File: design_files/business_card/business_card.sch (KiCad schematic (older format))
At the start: 32 parts, among them J1 Conn_01x06, J2 Conn_01x04_Male, SW3 SW_Push, SW4 SW_Push, U1 ATTINY85-20SU, U2 TLC5940PWP

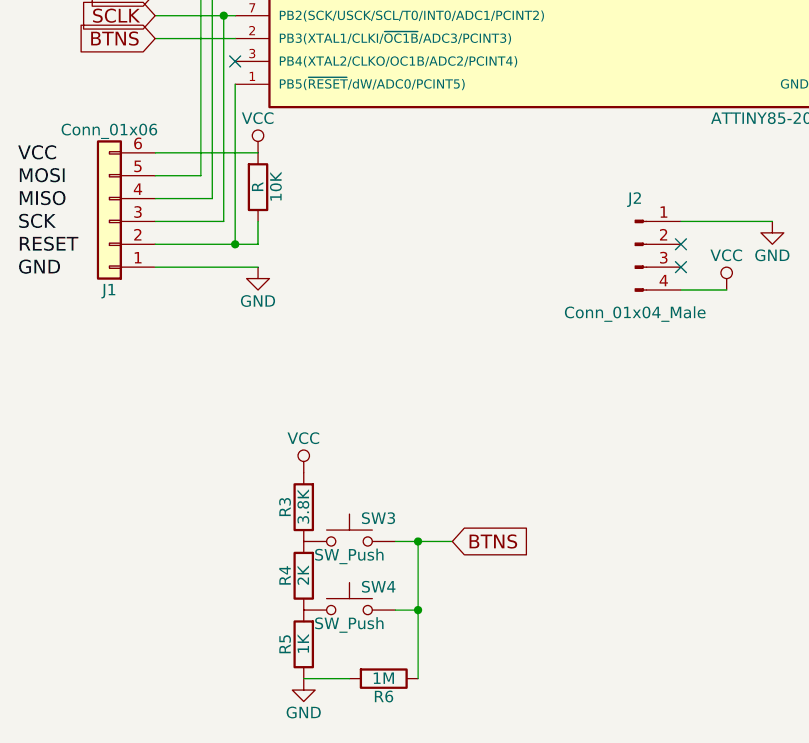
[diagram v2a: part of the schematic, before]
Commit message: progress on configuring 15 leds
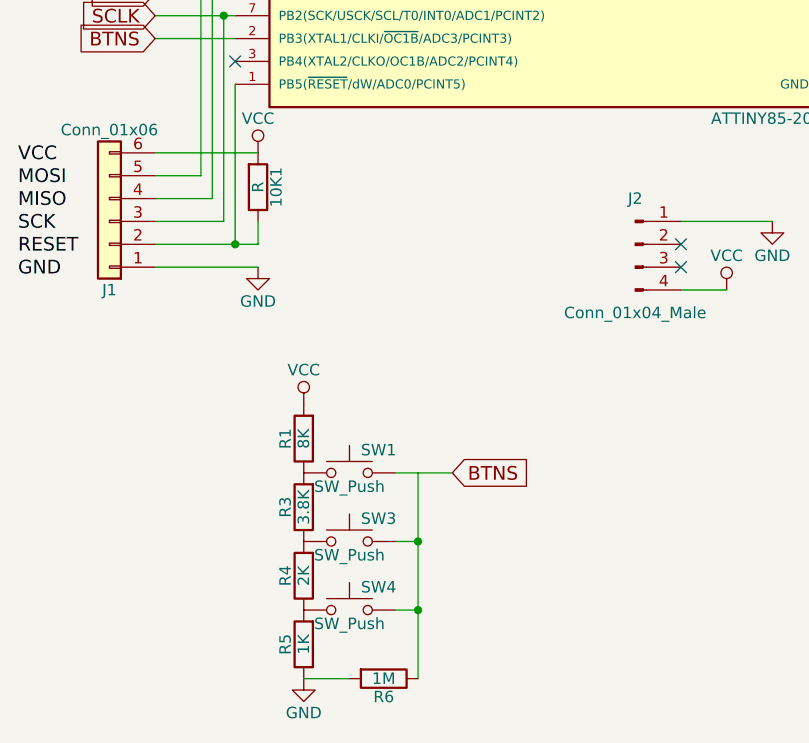
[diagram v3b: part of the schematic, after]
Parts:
- added R1: 8K, Resistors_SMD:R_0805, symbol R
- added SW1: SW_Push, Buttons_Switches_SMD:SW_SPST_SKQG, symbol SW_Push
- renumbered 10K to 10K1
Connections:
- net BTNS: now also SW1.2; no longer R6.1, SW3.2, SW4.2
- net VCC: now also R1.2; no longer R3.2
- new net: R6.1, SW3.2, SW4.2
- new net: R1.1, R3.2, SW1.1
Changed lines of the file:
@@
 $EndComp
 $Comp
-L VCC #PWR12
+L VCC #PWR01
 U 1 1 59C3E859
 P 10300 3400
-F 0 "#PWR12" H 10300 3250 50  0001 C CNN
+F 0 "#PWR01" H 10300 3250 50  0001 C CNN
 F 1 "VCC" H 10300 3550 50  0000 C CNN
 F 2 "" H 10300 3400 50  0001 C CNN
@@
 $EndComp
 $Comp
-L VCC #PWR10
+L VCC #PWR02
 U 1 1 59C443C0
 P 7550 2700
-F 0 "#PWR10" H 7550 2550 50  0001 C CNN
+F 0 "#PWR02" H 7550 2550 50  0001 C CNN
 F 1 "VCC" H 7550 2850 50  0000 C CNN
 F 2 "" H 7550 2700 50  0001 C CNN
@@
 $EndComp
 $Comp
-L GND #PWR11
+L GND #PWR03
 U 1 1 59C443FB
 P 7550 4850
-F 0 "#PWR11" H 7550 4600 50  0001 C CNN
+F 0 "#PWR03" H 7550 4600 50  0001 C CNN
 F 1 "GND" H 7550 4700 50  0000 C CNN
 F 2 "" H 7550 4850 50  0001 C CNN
@@
 BLANK
 $Comp
-L GND #PWR9
+L GND #PWR04
 U 1 1 59C4A413
 P 6150 3350
-F 0 "#PWR9" H 6150 3100 50  0001 C CNN
+F 0 "#PWR04" H 6150 3100 50  0001 C CNN
 F 1 "GND" H 6150 3200 50  0000 C CNN
 F 2 "" H 6150 3350 50  0001 C CNN
@@
 $EndComp
 $Comp
-L GND #PWR4
+L GND #PWR05
 U 1 1 59C62C72
 P 2350 6800
-F 0 "#PWR4" H 2350 6550 50  0001 C CNN
+F 0 "#PWR05" H 2350 6550 50  0001 C CNN
 F 1 "GND" H 2350 6650 50  0000 C CNN
 F 2 "" H 2350 6800 50  0001 C CNN
@@
 $EndComp
 $Comp
-L VCC #PWR3
+L VCC #PWR06
 U 1 1 59C62D86
-P 2350 5900
-F 0 "#PWR3" H 2350 5750 50  0001 C CNN
-F 1 "VCC" H 2350 6050 50  0000 C CNN
-F 2 "" H 2350 5900 50  0001 C CNN
-F 3 "" H 2350 5900 50  0001 C CNN
-	1    2350 5900
+P 2350 5600
+F 0 "#PWR06" H 2350 5450 50  0001 C CNN
+F 1 "VCC" H 2350 5750 50  0000 C CNN
+F 2 "" H 2350 5600 50  0001 C CNN
+F 3 "" H 2350 5600 50  0001 C CNN
+	1    2350 5600
 	1    0    0    -1
 $EndComp
 Text GLabel 1700 4000 0    60   Input ~ 0
 BTNS
-Text GLabel 3000 6200 2    60   Input ~ 0
+Text GLabel 3000 5900 2    60   Input ~ 0
 BTNS
 NoConn ~ 7450 4800
@@
 NoConn ~ 6850 4500
 $Comp
-L GND #PWR8
+L GND #PWR07
 U 1 1 59C66F52
 P 4850 4200
-F 0 "#PWR8" H 4850 3950 50  0001 C CNN
+F 0 "#PWR07" H 4850 3950 50  0001 C CNN
 F 1 "GND" H 4850 4050 50  0000 C CNN
 F 2 "" H 4850 4200 50  0001 C CNN
@@
 GND
 $Comp
-L VCC #PWR1
+L VCC #PWR08
 U 1 1 59C6C0D5
 P 2150 4500
-F 0 "#PWR1" H 2150 4350 50  0001 C CNN
+F 0 "#PWR08" H 2150 4350 50  0001 C CNN
 F 1 "VCC" H 2150 4650 50  0000 C CNN
 F 2 "" H 2150 4500 50  0001 C CNN
@@
 NoConn ~ 4000 5000
 $Comp
-L VCC #PWR5
+L VCC #PWR09
 U 1 1 59C7428C
 P 4200 5100
-F 0 "#PWR5" H 4200 4950 50  0001 C CNN
+F 0 "#PWR09" H 4200 4950 50  0001 C CNN
 F 1 "VCC" H 4200 5250 50  0000 C CNN
 F 2 "" H 4200 5100 50  0001 C CNN
@@
 $EndComp
 $Comp
-L GND #PWR6
+L GND #PWR010
 U 1 1 59C7439F
 P 4400 4800
-F 0 "#PWR6" H 4400 4550 50  0001 C CNN
+F 0 "#PWR010" H 4400 4550 50  0001 C CNN
 F 1 "GND" H 4400 4650 50  0000 C CNN
 F 2 "" H 4400 4800 50  0001 C CNN
@@
 $EndComp
 $Comp
-L VCC #PWR7
+L VCC #PWR011
 U 1 1 59C54A1F
 P 4850 3700
-F 0 "#PWR7" H 4850 3550 50  0001 C CNN
+F 0 "#PWR011" H 4850 3550 50  0001 C CNN
 F 1 "VCC" H 4850 3850 50  0000 C CNN
 F 2 "" H 4850 3700 50  0001 C CNN
@@
 Wire Wire Line
 	2550 6800 2350 6800
-Wire Wire Line
-	2750 6200 3000 6200
 Connection ~ 2850 6200
 Wire Wire Line
@@
 	2150 4500 1700 4500
 $Comp
-L GND #PWR?
+L GND #PWR012
 U 1 1 59EAB901
 P 2150 5000
-F 0 "#PWR?" H 2150 4750 50  0001 C CNN
+F 0 "#PWR012" H 2150 4750 50  0001 C CNN
 F 1 "GND" H 2150 4850 50  0000 C CNN
 F 2 "" H 2150 5000 50  0001 C CNN
@@
 Connection ~ 1900 3700
 $Comp
-L R 10K
+L R 10K1
 U 1 1 59EAD6BF
 P 2150 4650
-F 0 "10K" V 2230 4650 50  0000 C CNN
+F 0 "10K1" V 2230 4650 50  0000 C CNN
 F 1 "R" V 2150 4650 50  0000 C CNN
 F 2 "Resistors_SMD:R_0805" V 2080 4650 50  0001 C CNN
@@
 $EndComp
 Wire Wire Line
-	2850 6200 2850 6800
+	2850 5900 2850 6800
+$Comp
+L SW_Push SW1
+U 1 1 59ED4393
+P 2550 5900
+F 0 "SW1" H 2600 6000 50  0000 L CNN
+F 1 "SW_Push" H 2550 5840 50  0000 C CNN
+F 2 "Buttons_Switches_SMD:SW_SPST_SKQG" H 2550 6100 50  0001 C CNN
+F 3 "" H 2550 6100 50  0001 C CNN
+	1    2550 5900
+	1    0    0    -1
+$EndComp
+Wire Wire Line
+	2750 6200 2850 6200
+Wire Wire Line
+	2750 5900 3000 5900
+$Comp
+L R R1
+U 1 1 59ED464F
+P 2350 5750
+F 0 "R1" V 2430 5750 50  0000 C CNN
+F 1 "8K" V 2350 5750 50  0000 C CNN
+F 2 "Resistors_SMD:R_0805" V 2280 5750 50  0001 C CNN
+F 3 "" H 2350 5750 50  0001 C CNN
+	1    2350 5750
+	-1   0    0    1
+$EndComp
 $EndSCHEMATC
